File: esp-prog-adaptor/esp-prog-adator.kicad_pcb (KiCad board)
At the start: 2 copper layers, 40.6 x 55.9 mm, 6 parts, among them J1 Conn_02x19_Odd_Even, J2 Conn_02x19_Odd_Even

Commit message: 레이블 정리
Signed-off-by: Ju, Gyeong-min <jcmh74@gmail.com>
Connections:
- net /IO0 renamed /G00
- net /TCK(IO13) renamed /TCK(G13)
- net /TDI(IO12) renamed /TDI(G12)
- net /TDO(IO15) renamed /TDO(G15)
- net /TMS(IO14) renamed /TMS(G14)
- net /VCC1 renamed /Vjtag
- net /VCC2 renamed /Vprog

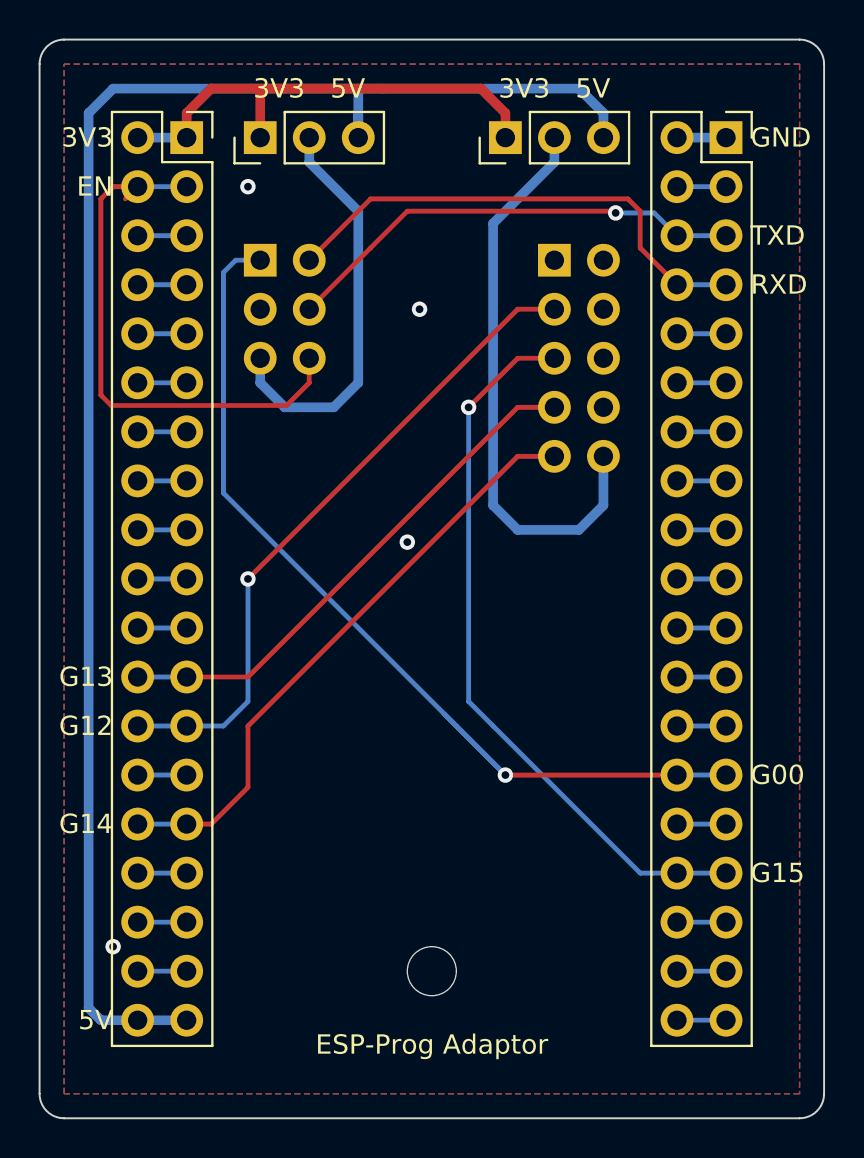
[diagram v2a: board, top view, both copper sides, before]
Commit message: 핀 번호 실수 수정
Signed-off-by: Ju, Gyeong-min <jcmh74@gmail.com>
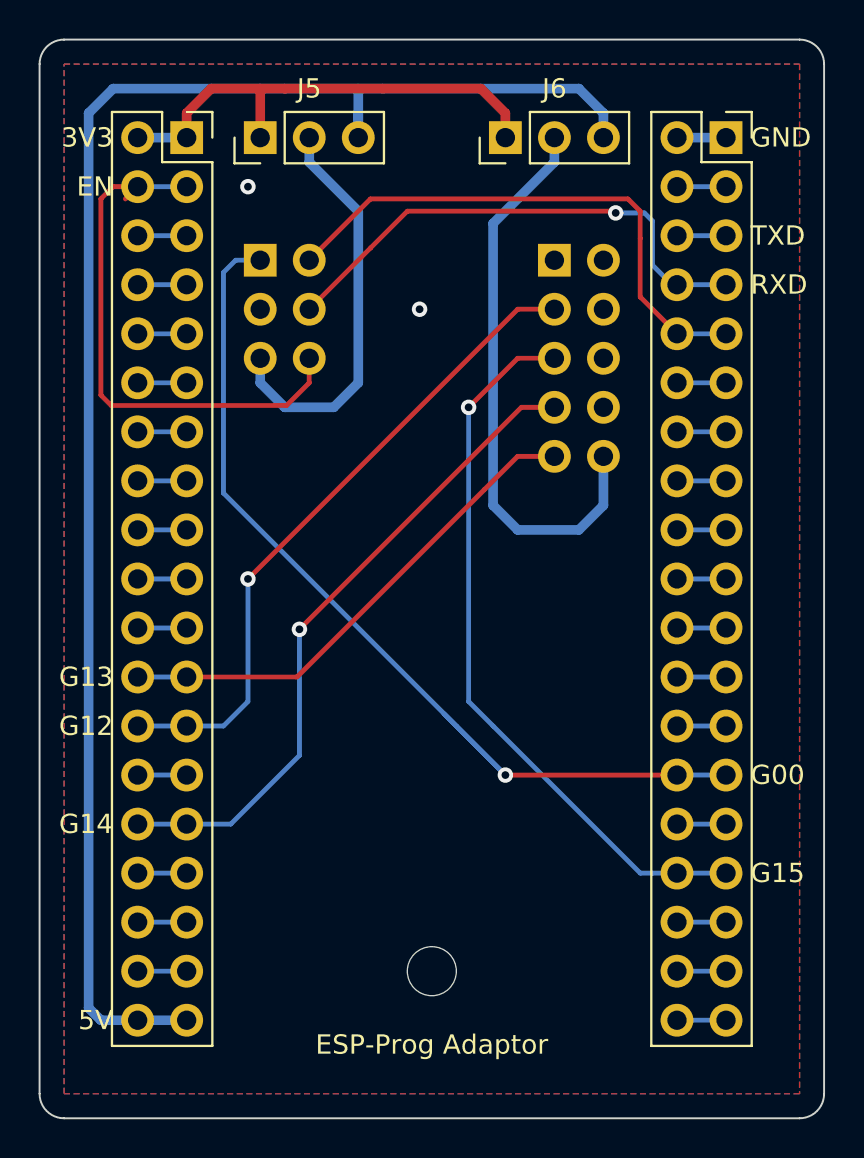
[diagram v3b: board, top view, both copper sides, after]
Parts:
- J5, J6: renamed from 3V3   5V
- renumbered JTAG to JTAG1, PROG to PROG1
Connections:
- J1 pad 23: /TCK(G13) -> /TMS(G14)
- J1 pad 24: /TCK(G13) -> /TMS(G14)
- J1 pad 29: /TMS(G14) -> /TCK(G13)
- J1 pad 30: /TMS(G14) -> /TCK(G13)
- J2 pad 10: Net-(J2-Pad10) -> /RXD
- J2 pad 5: /TXD -> Net-(J2-Pad5)
- J2 pad 6: /TXD -> Net-(J2-Pad5)
- J2 pad 7: /RXD -> /TXD
- J2 pad 8: /RXD -> /TXD
- J2 pad 9: Net-(J2-Pad10) -> /RXD
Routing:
- net /TCK(G13): track 27.4 -> 34.4 mm, vias 0 -> 1
- net /TMS(G14): track 31.3 -> 26.3 mm
- net /TXD: track 24.2 -> 27.0 mm, vias 2 -> 1
- net /RXD: track 25.9 -> 28.4 mm
- net Net-(J2-Pad5): track 0.00 -> 2.54 mm
- net Net-(J2-Pad10): track 2.54 -> 0.00 mm
- net GND: vias 4 -> 2

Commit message: 디버거 연결 케넥터 위치 미세 조정
Signed-off-by: Ju, Gyeong-min <jcmh74@gmail.com>
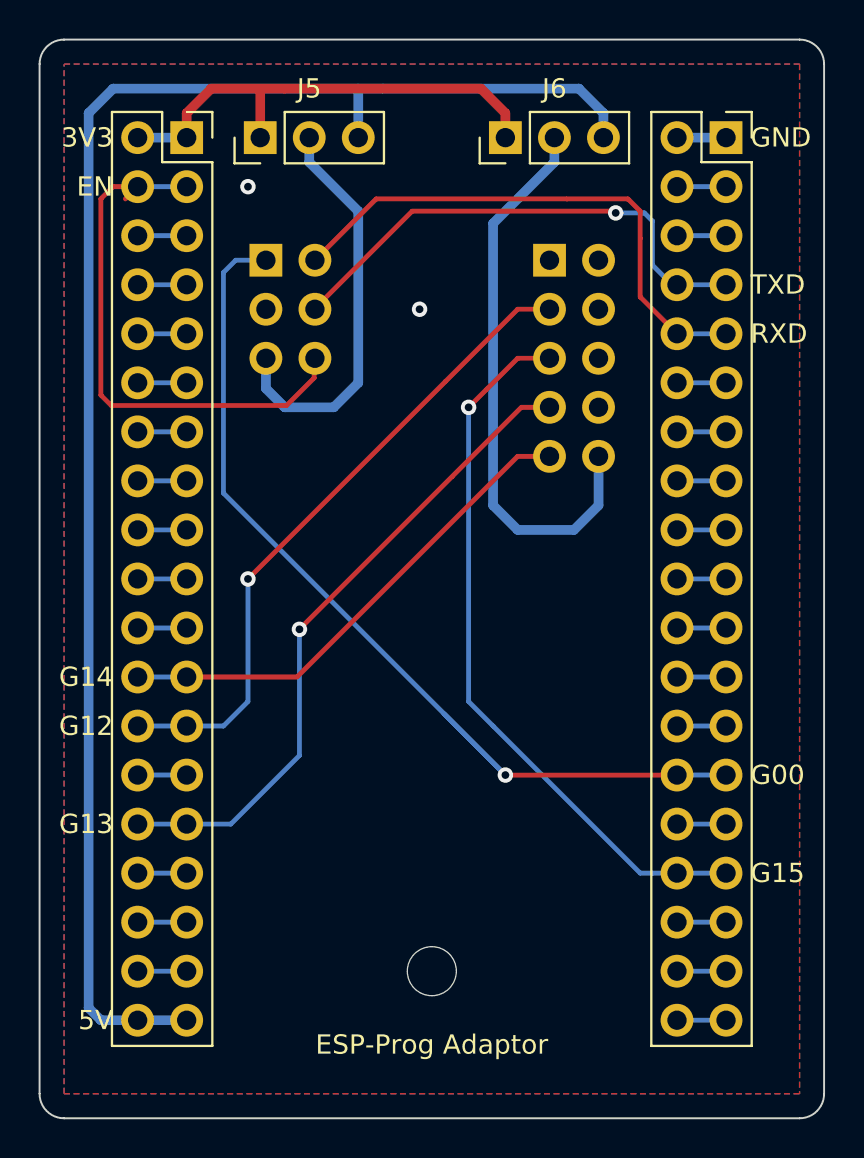
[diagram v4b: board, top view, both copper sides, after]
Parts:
- moved PROG1 0.29 mm to (90.5, 77.5)
- moved JTAG1 0.25 mm to (105.2, 77.5)
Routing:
- net /Vjtag: track 32.0 -> 29.4 mm
- net +5V: track 84.5 -> 83.2 mm
